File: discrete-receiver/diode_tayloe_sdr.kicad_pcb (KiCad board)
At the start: 4 copper layers, 110 x 110 mm, 268 parts, among them J2 Optional 5V DC Jack, J3 External Filter, J4 Debug Pins, J5 Display Connector, J6 SI-52003-F, T1 H1102NLT, T2 MABA-007159-000000, U1 SN74CBT3253DBQR, U10 MS5351M, U11 Ag9905LP, U13 LM66100DCK, U14 LM66100DCK, U15 LM66100DCK, U16 PSA4-5043_, U2 OPA1612AxD, U3 OPA1612AxD, U4 CJC5340, U5 ADE-1+, U6 RP2350A, U7 W25Q128, U9 LAN8720A, X1 YC24.576MUBCE2O, X2 X322512MSB4SI

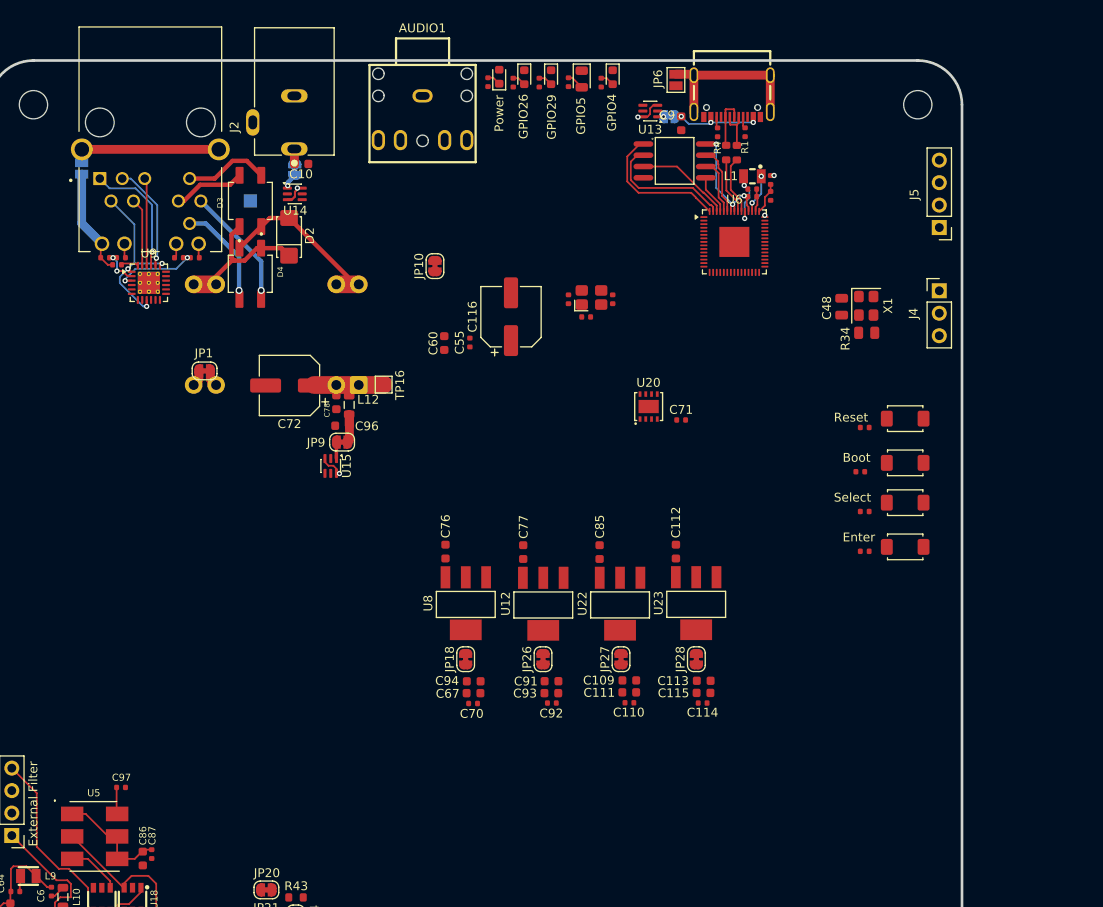
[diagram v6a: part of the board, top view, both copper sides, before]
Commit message: PCB Progress
Moved rp2350 and Ethernet hardware closer together, drew 50MHz clock line from rp2350 to LAN8720 with via stitching
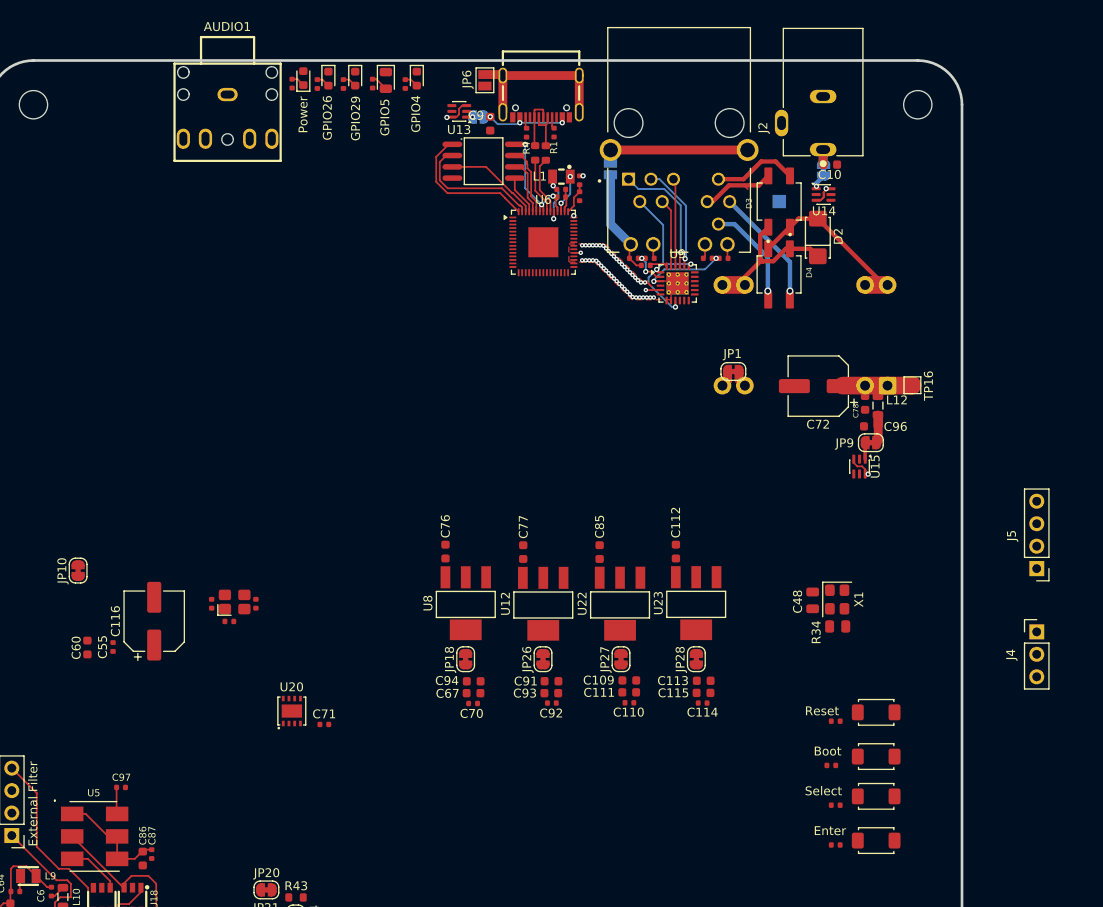
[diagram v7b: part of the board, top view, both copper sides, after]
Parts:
- moved TP16 59.8 mm to (136.9, 68.2)
- moved U11 59.8 mm to (134.1, 68.3)
- moved C10 59.8 mm to (127.6, 43.3)
- moved C72 59.8 mm to (126.2, 68.3)
- moved D3 59.8 mm to (121.8, 47.5)
- moved D4 59.8 mm to (121.8, 55.7)
- moved J2 59.8 mm to (126.8, 35.1)
- moved J6 59.8 mm to (110.5, 41.6)
- moved JP5 59.8 mm to (102.7, 43.8)
- moved JP8 59.8 mm to (126.8, 43.9)
- moved L12 59.8 mm to (133.0, 70.5)
- moved R18 59.8 mm to (106.7, 54.7)
- moved R30 59.8 mm to (115.5, 53.9)
- moved R33 59.8 mm to (113.7, 53.9)
- moved TP8 59.8 mm to (121.8, 47.5)
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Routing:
- net /Ethernet Interface/50 MHz Clk: track 0.00 -> 11.5 mm, vias 0 -> 2
- net +3.3V: track 43.5 -> 51.2 mm
- net GND: track 18.6 -> 19.5 mm, vias 0 -> 47
- net POE A1: track 8.12 -> 8.70 mm
- added copper zone on F.Cu, net GND
- added copper zone on In1.Cu, net GND
- added copper zone on In2.Cu, net GND
